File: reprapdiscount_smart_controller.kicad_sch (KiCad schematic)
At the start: 36 parts, among them J1 USB_A, Q1 BC817, Q2 BC817, U1 74HC4050, U3 Pico

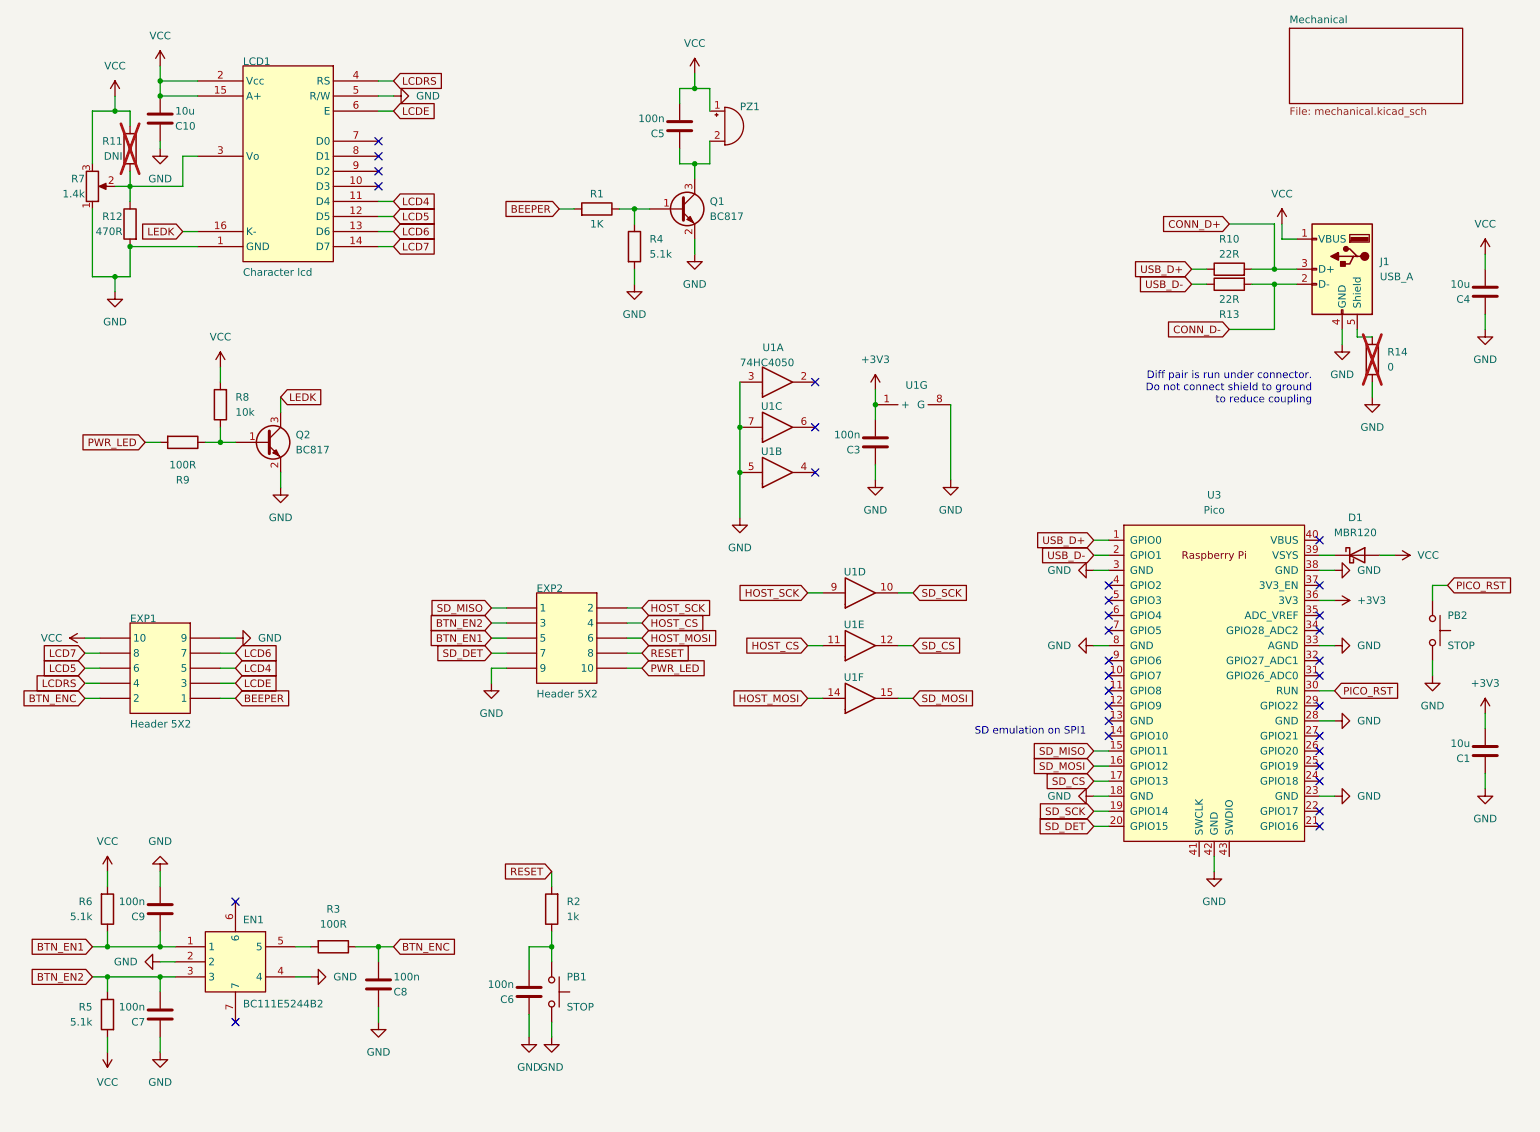
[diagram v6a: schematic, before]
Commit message: feature: add status leds to pico
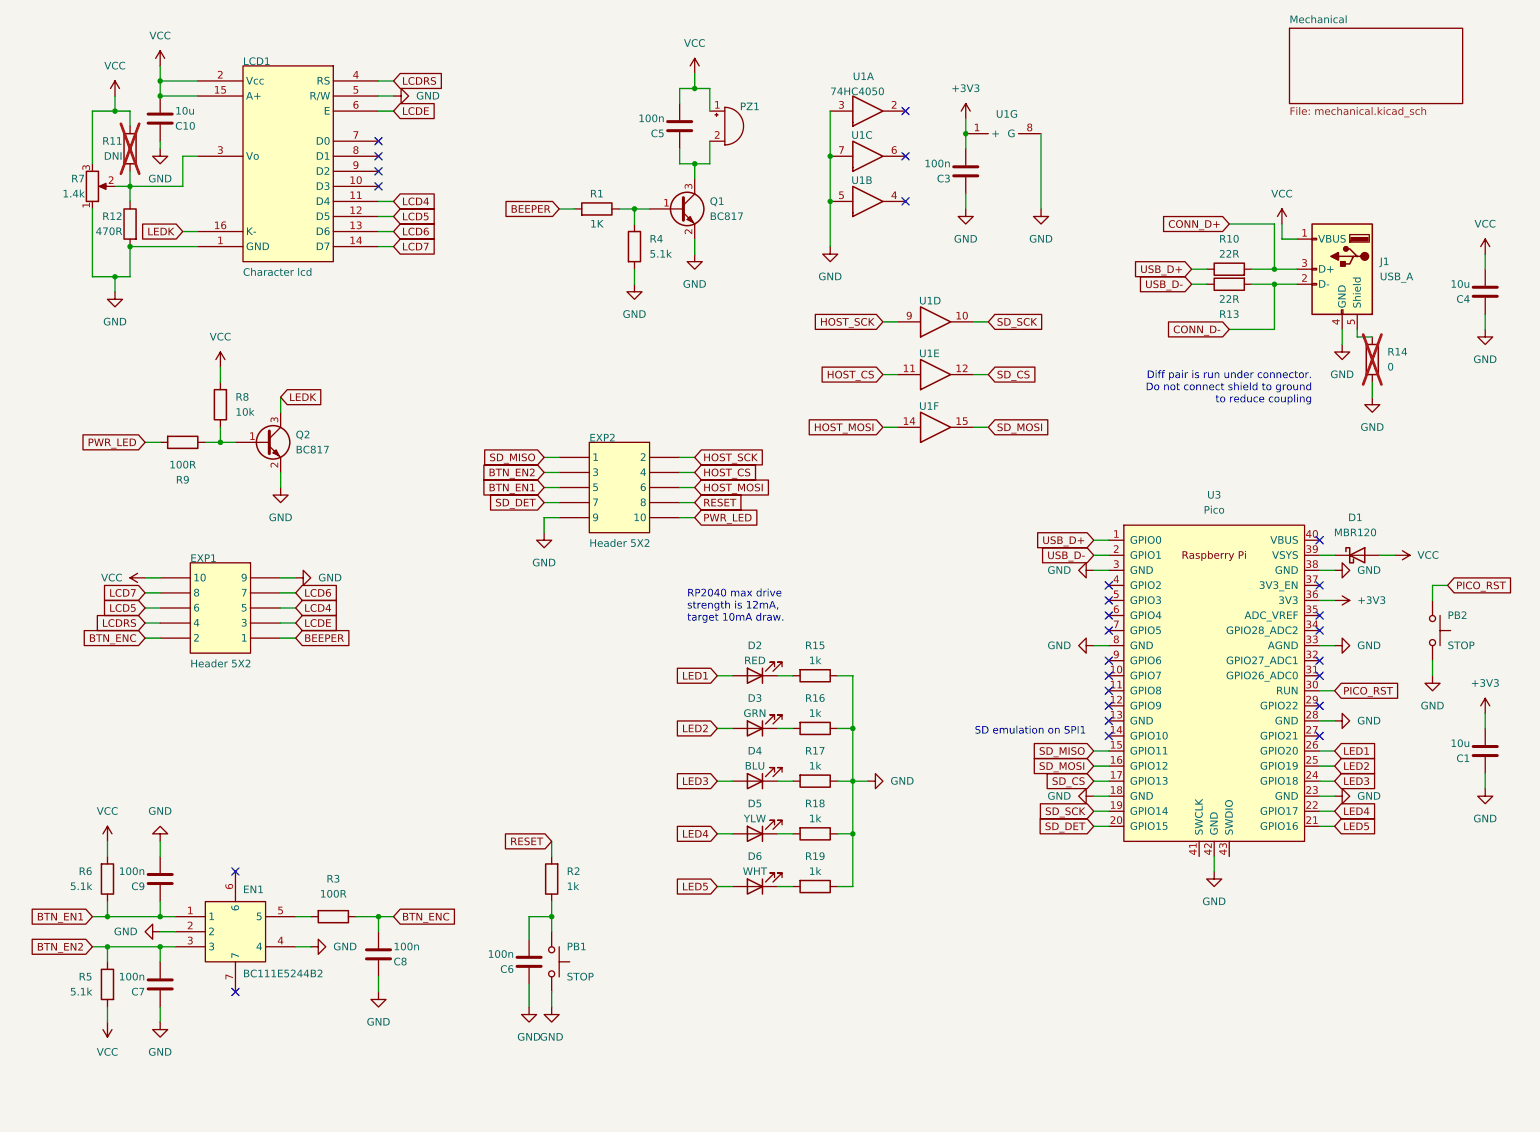
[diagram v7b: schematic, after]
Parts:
- added D2: RED, LED_SMD:LED_0805_2012Metric_Pad1.15x1.40mm_HandSolder, symbol Device:LED
- added D3: GRN, LED_SMD:LED_0805_2012Metric_Pad1.15x1.40mm_HandSolder, symbol Device:LED
- added D4: BLU, LED_SMD:LED_0805_2012Metric_Pad1.15x1.40mm_HandSolder, symbol Device:LED
- added D5: YLW, LED_SMD:LED_0805_2012Metric_Pad1.15x1.40mm_HandSolder, symbol Device:LED
- added D6: WHT, LED_SMD:LED_0805_2012Metric_Pad1.15x1.40mm_HandSolder, symbol Device:LED
- added R15, R16, R17, R18, R19: 1k, Resistor_SMD:R_0805_2012Metric_Pad1.20x1.40mm_HandSolder, symbol Device:R
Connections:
- net GND: now also R15.1, R16.1, R17.1, R18.1, R19.1
- net LED5: now reaches U3.21 (GPIO16)
- net LED5: now also D6.2 (A)
- net LED4: now reaches U3.22 (GPIO17)
- net LED4: now also D5.2 (A)
- net LED3: now reaches U3.24 (GPIO18)
- net LED3: now also D4.2 (A)
- net LED2: now reaches U3.25 (GPIO19)
- net LED2: now also D3.2 (A)
- net LED1: now reaches U3.26 (GPIO20)
- net LED1: now also D2.2 (A)
- new net: D3.1 (K), R16.2
- new net: D4.1 (K), R17.2
- new net: D2.1 (K), R15.2
- new net: D6.1 (K), R19.2
- new net: D5.1 (K), R18.2
- no-connect marks 32 -> 27
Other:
- note added: "RP2040 max drive strength is 12mA, target 10mA draw."
- moved on the sheet: C3, C6, C7, C8, C9, EN1, EXP1, EXP2, PB1, R2, R3, R5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

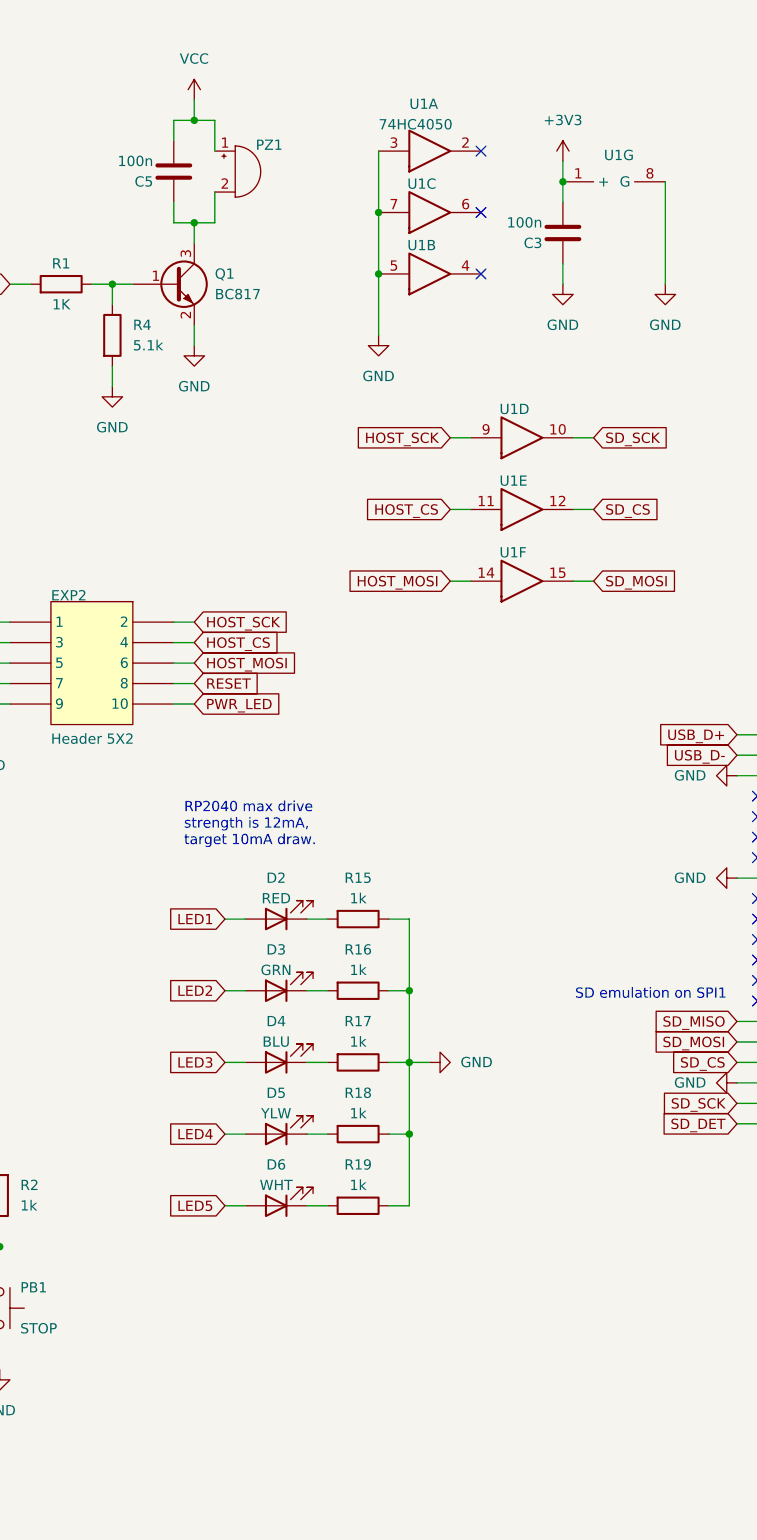
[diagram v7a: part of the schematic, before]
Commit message: feature: use buffer to drive leds
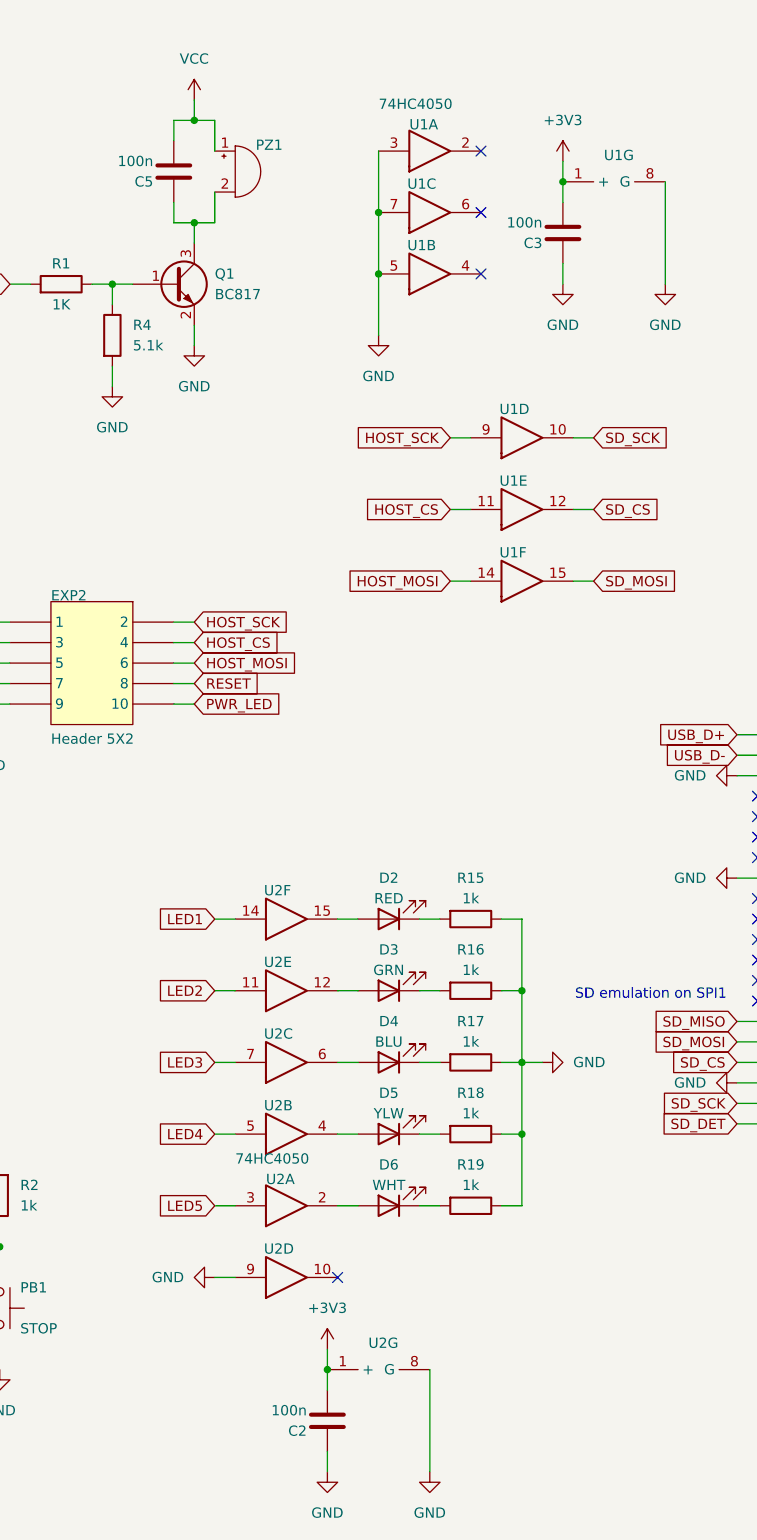
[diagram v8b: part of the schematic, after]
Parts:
- added C2: 100n, Capacitor_SMD:C_0805_2012Metric_Pad1.18x1.45mm_HandSolder, symbol Device:C
- added U2: 74HC4050, reprapdiscount_smart_controller:SO-16_3.9x9.9mm_P1.27mm, symbol reprapdiscount_smart_controller-altium-import:root_0_74HC4050
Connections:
- net +3V3: now also C2.2, U2.1 (+)
- net GND: now also C2.1, U2.8 (G), U2.9
- net LED1: now also U2.14; no longer D2.2 (A)
- net LED2: now also U2.11; no longer D3.2 (A)
- net LED3: now also U2.7; no longer D4.2 (A)
- net LED4: now also U2.5; no longer D5.2 (A)
- net LED5: now also U2.3; no longer D6.2 (A)
- new net: D3.2 (A), U2.12
- new net: D2.2 (A), U2.15
- new net: D4.2 (A), U2.6
- new net: D6.2 (A), U2.2
- new net: D5.2 (A), U2.4
- no-connect marks 27 -> 28
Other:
- note removed: "RP2040 max drive strength is 12mA, target 10mA draw."
- moved on the sheet: D2, D3, D4, D5, D6, R15, R16, R17, R18, R19
